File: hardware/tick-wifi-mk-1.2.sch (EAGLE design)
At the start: 25 parts, among them IC1 MAX7219, IC2 MAX7219, IC3 74HC125, IC4 LD1117 5V, U1 Adafruit Feather HUZZAH ESP82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

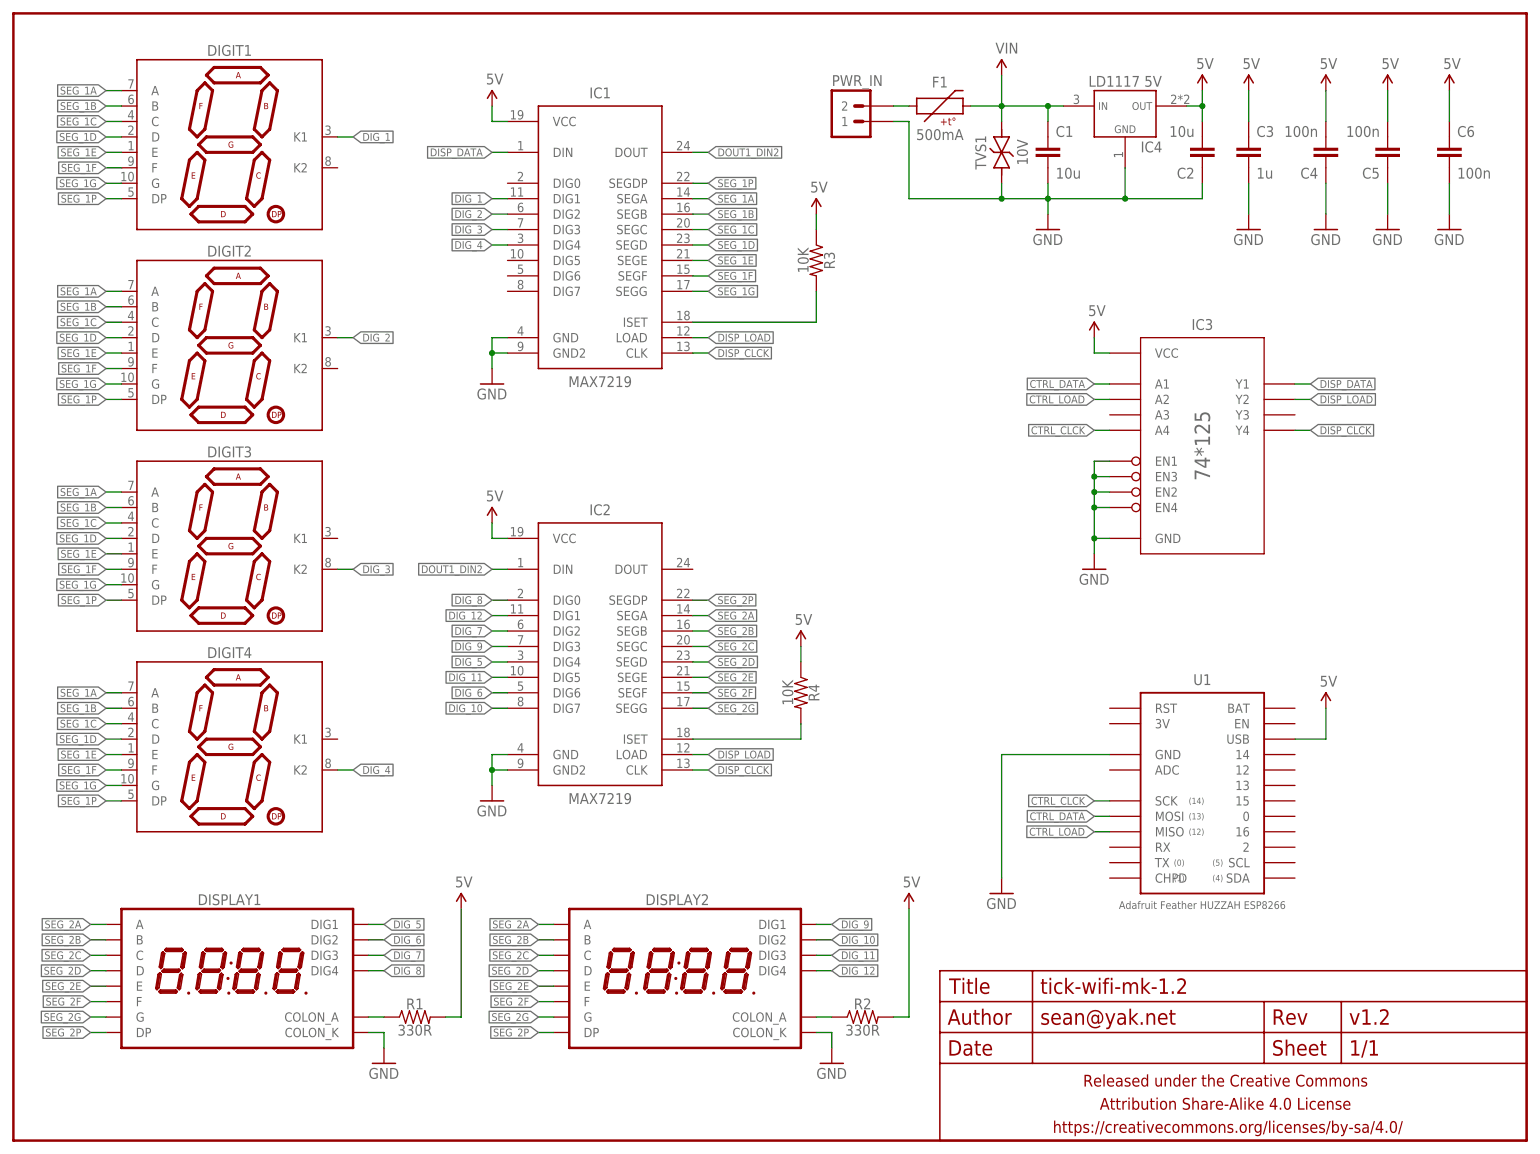
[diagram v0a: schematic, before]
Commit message: fucking silkscreen error--flipped CLK and DAT markings
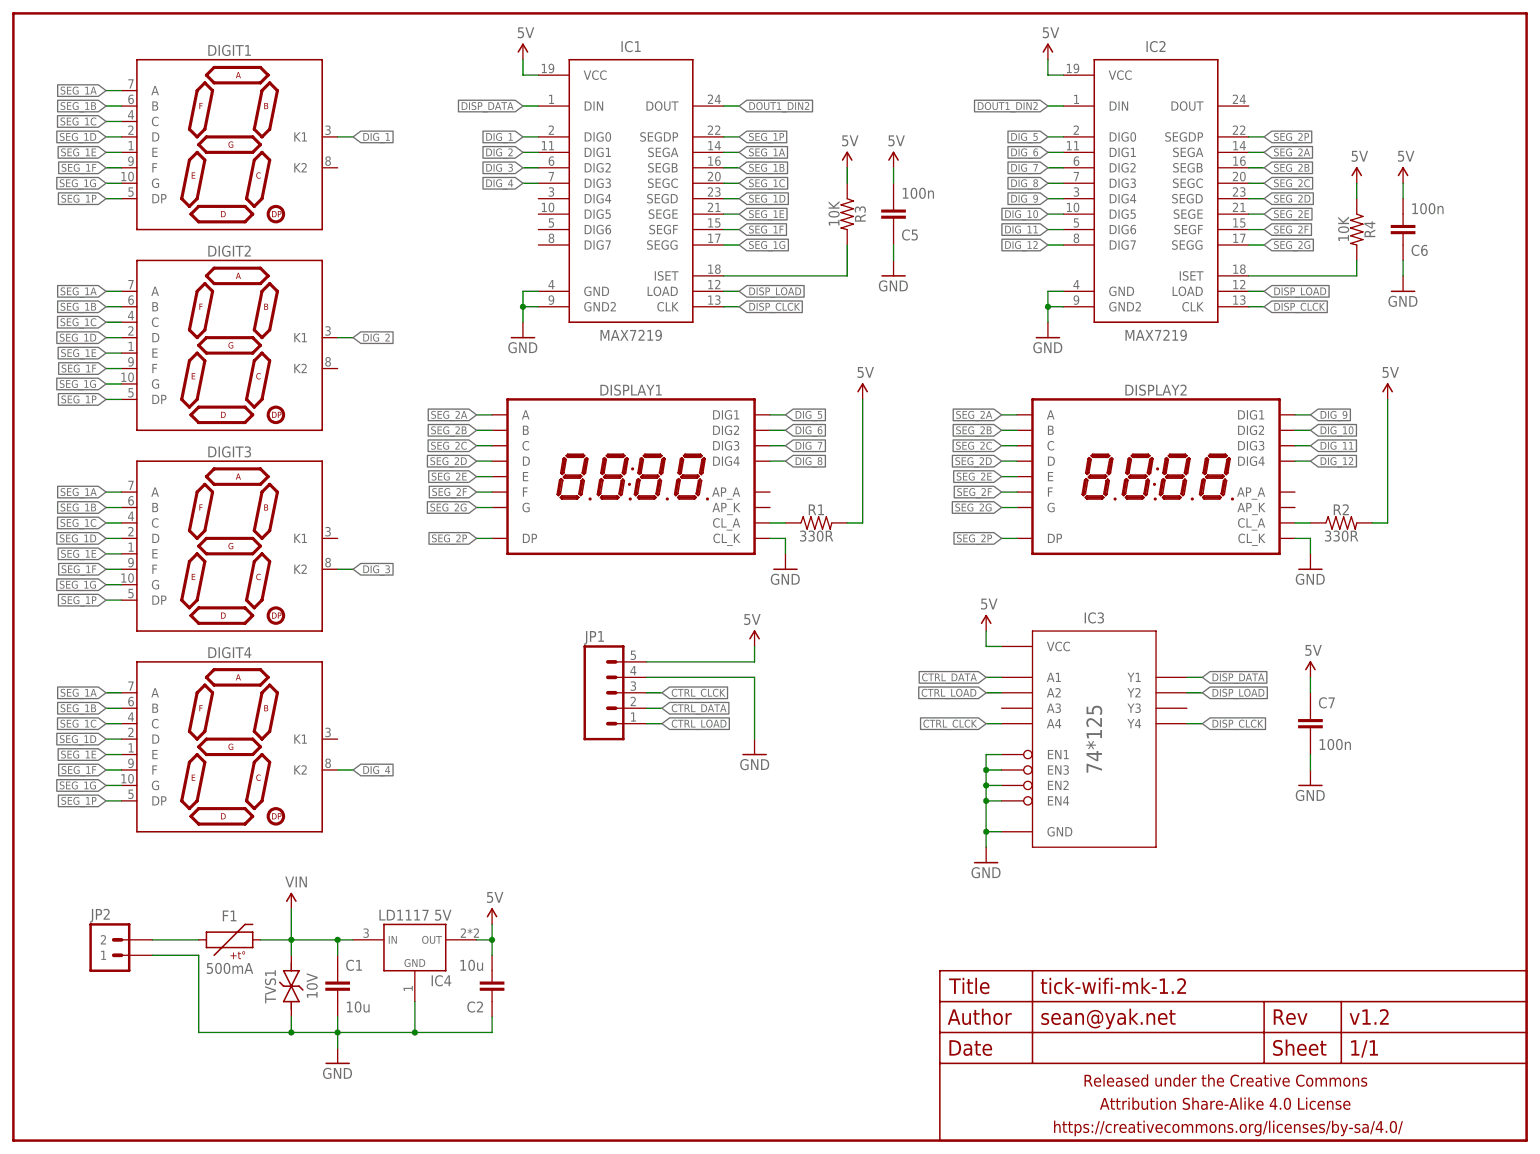
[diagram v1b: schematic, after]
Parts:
- removed C3: 1u, a_parts:CAPACITOR-CERAMICC0805
- removed C4: 100n, a_parts:CAPACITOR-CERAMICC0603
- removed PWR_IN: M02PTH-CENTERED-R+, A_butts:M02PTH-CENTERED-R+
- removed U1: Adafruit Feather HUZZAH ESP8266, a_parts:ADAFRUIT_FEATHER_HUZZAH_ESP8266
- added C7: 100n, a_parts:CAPACITOR-CERAMICC0603
- added JP1: M05PTH-CENTERED, a_parts:M05PTH-CENTERED
- added JP2: M02PTH-CENTERED-R+, a_parts:M02PTH-CENTERED-R+
- DIGIT1, DIGIT2, DIGIT3, DIGIT4: device A_butts:7SEG_1DIGPTH-25.4MM-BARE -> a_parts:7SEG_1DIGPTH-25.4MM-BARE
- DISPLAY1, DISPLAY2: value 7SEG_4DIGIT_COLON14.2MM-CC -> 7SEG_4DIGIT_COLON_APOS; device a_parts:7SEG_4DIGIT_COLON14.2MM-CC -> a_parts:7SEG_4DIGIT_COLON_APOS
- F1: device A_butts:PTCPTC-1210 -> a_parts:PTCPTC-1210
- FRAME1: device A_butts:FRAME-LETTERNO_PACKAGE -> a_parts:FRAME-LETTERNO_PACKAGE
- R1, R2: device a_parts:RESISTORR0805 -> a_parts:RESISTORR0603
- TVS1: device A_butts:TVSSMA -> a_parts:TVSSMA
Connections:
- net 5V: now also C6.2, C7.1, JP1.5; no longer C3.1, C4.2, C6.1, U1.USB
- net CTRL_CLCK: now also JP1.3; no longer U1.SCK
- net CTRL_DATA: now also JP1.2; no longer U1.MOSI
- net CTRL_LOAD: now also JP1.1; no longer U1.MISO
- net DIG_1: now also IC1.DIG0; no longer IC1.DIG1
- net DIG_10: now also IC2.DIG5; no longer IC2.DIG7
- net DIG_11: now also IC2.DIG6; no longer IC2.DIG5
- net DIG_12: now also IC2.DIG7; no longer IC2.DIG1
- net DIG_2: now also IC1.DIG1; no longer IC1.DIG2
- net DIG_3: now also IC1.DIG2; no longer IC1.DIG3
- net DIG_4: now also IC1.DIG3; no longer IC1.DIG4
- net DIG_5: now also IC2.DIG0; no longer IC2.DIG4
- net DIG_6: now also IC2.DIG1; no longer IC2.DIG6
- net DIG_8: now also IC2.DIG3; no longer IC2.DIG0
- net DIG_9: now also IC2.DIG4; no longer IC2.DIG3
- net GND: now also C6.1, C7.2, DISPLAY1.CL_K, DISPLAY2.CL_K, JP1.4, JP2.1; no longer C3.2, C4.1, C6.2, DISPLAY1.COLON_K, DISPLAY2.COLON_K, PWR_IN.1, U1.GND
- net N$1: now also JP2.2; no longer PWR_IN.2
- net N$3: now also DISPLAY1.CL_A; no longer DISPLAY1.COLON_A
- net N$5: now also DISPLAY2.CL_A; no longer DISPLAY2.COLON_A
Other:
- moved on the sheet: C1, C2, C5, C6, F1, IC1, IC2, IC3, IC4, R1, R2, R3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
